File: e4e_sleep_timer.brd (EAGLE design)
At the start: 160 x 100 mm, 26 parts, among them P1 XT60, P2 10129378-906001BLF, P3 XT30PW-F, Q1 PJA3416AE_R1_00001, U1 NUCLEO-G071RB, U2 1224-5-150W

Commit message: Finished PCB review
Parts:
- removed U$5: FH-320-NV, fuses:FH-320-NV
- added Q2: PJA3416AE_R1_00001, PJA3416AE_R1_00001:SOT23_PJA3416_PNJ
- added R6: 0, rcl:R0603
- added TP11, TP12, TP13, TP14: TPTP20R, testpad:TP20R
- added U5: FH-320-NV, fuses:FH-320-NV
- moved R2 66.3 mm to (83.8, 21.6)
- moved R1 66.1 mm to (83.8, 19.1)
- moved TP8 66.0 mm to (80.0, 96.5)
- moved TP3 58.4 mm to (83.8, 96.5)
- moved U$3 53.3 mm to (101.6, 95.2)
- moved U$4 53.3 mm to (101.6, 5.08)
- moved U2 52.8 mm to (105.4, 67.3)
- moved P3 52.6 mm to (105.4, 33.0)
- moved P2 52.6 mm to (103.6, 17.8), turned to 90 degrees
- moved TP2 50.8 mm to (87.6, 96.5)
- moved TP1 43.2 mm to (91.4, 96.5)
- moved R4 40.1 mm to (85.1, 27.9), turned to 270 degrees
- moved Q1 39.9 mm to (90.2, 31.8)
- moved R3 39.3 mm to (86.0, 31.5)
- moved R5 38.6 mm to (82.5, 27.9), turned to 90 degrees
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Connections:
- removed net U5V: U1.CN10_8
- removed net VBAT: U1.CN7_33
- removed net VIN_S1: U1.CN7_24
- new net N$6: TP11.TP, U1.CN7_24
- new net N$7: R6.1, U1.CN10_32, U1.CN10_9
- new net N$8: TP13.TP, U1.CN10_8
- new net N$9: TP14.TP, U1.CN7_33
- net +5V: now also U5.2; no longer U$5.2
- net GND: now also R6.2; no longer U1.CN10_32, U1.CN10_9
- net N$2: now also Q2.1
- net N$5: now also Q2.3, TP12.TP, U5.1; no longer U$5.1
- net VDD1: now also Q2.2
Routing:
- net USART1_RXD: track 87.5 -> 10.4 mm
- net USART1_TXD: track 86.1 -> 25.4 mm
- net N$7: track 0.00 -> 54.0 mm
- net +5V: track 195.9 -> 157.1 mm
- net SYS_PWR: track 66.0 -> 29.3 mm, vias 0 -> 1
- net N$1: track 65.4 -> 37.9 mm
- net N$5: track 2.78 -> 24.4 mm
- net VEXT: track 50.1 -> 28.9 mm
- net N$8: track 0.00 -> 16.8 mm
- net N$3: track 5.63 -> 19.0 mm
- net N$6: track 0.00 -> 9.25 mm
- net N$9: track 0.00 -> 6.62 mm
- net N$2: track 4.39 -> 10.6 mm, vias 0 -> 2
- net N$4: track 7.37 -> 5.25 mm
- net VDD1: track 88.7 -> 90.5 mm
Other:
- board size 160 x 100 mm -> 107.9 x 100 mm
- board text added: "REV A"
- board text added: "Sleep Timer Board"

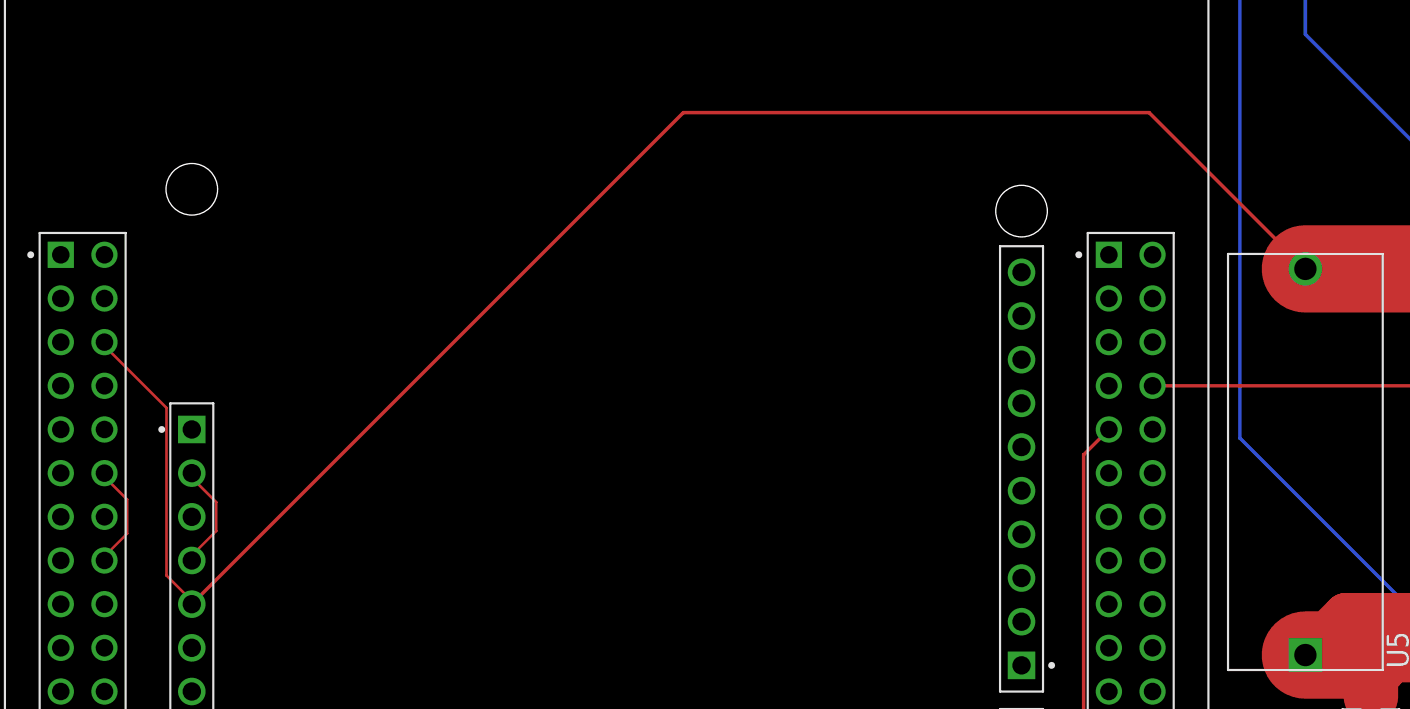
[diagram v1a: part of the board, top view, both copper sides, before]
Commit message: Added Nucleo Board power bypass
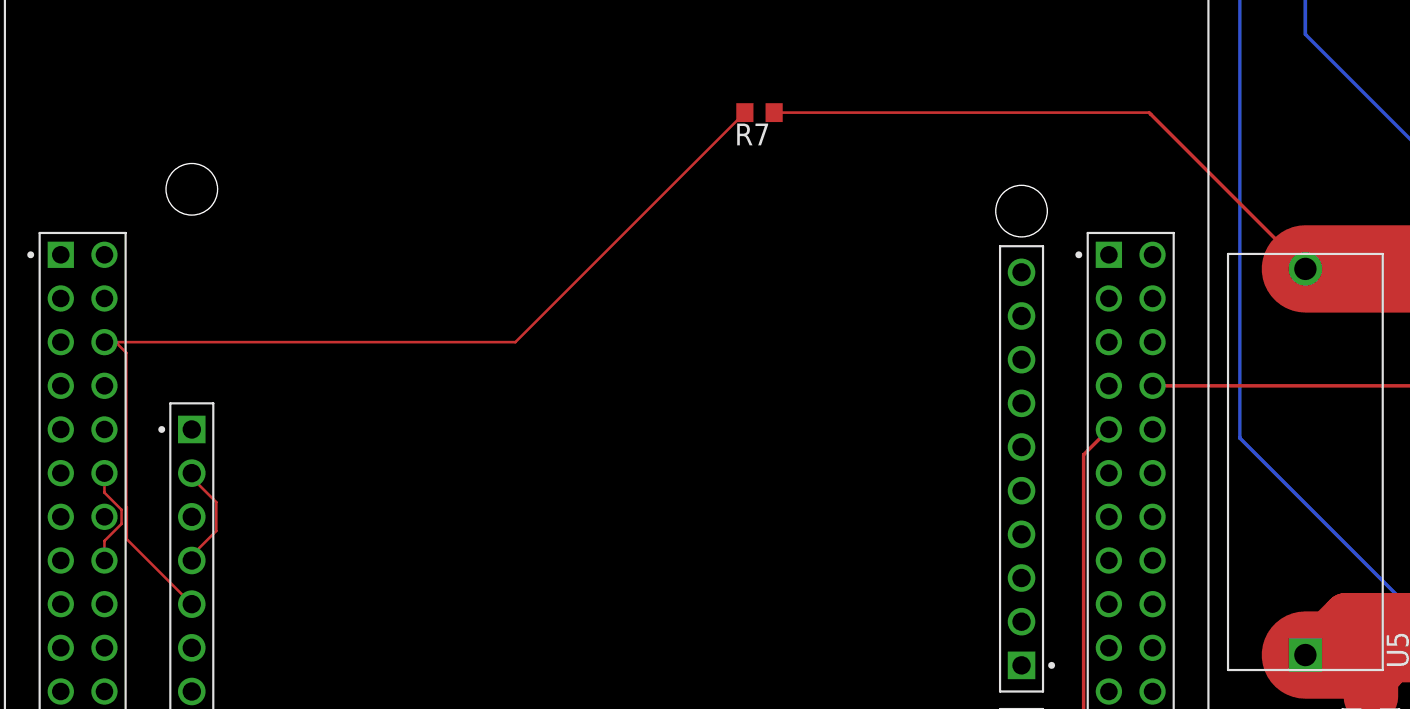
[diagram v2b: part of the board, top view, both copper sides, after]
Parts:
- added R7: 0, rcl:R0603
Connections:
- new net VDD2: R7.2, U1.CN6_5, U1.CN7_6
- net +5V: now also R7.1; no longer U1.CN6_5, U1.CN7_6
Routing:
- net +5V: track 157.1 -> 93.9 mm
- net VDD2: track 0.00 -> 60.5 mm
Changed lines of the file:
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@@
 <attribute name="VALUE" x="6.858" y="18.034" size="0.0254" layer="27"/>
+</element>
+<element name="R7" library="rcl" library_urn="urn:adsk.eagle:library:334" package="R0603" package3d_urn="urn:adsk.eagle:package:23555/3" value="0" x="54.61" y="67.31" smashed="yes" rot="R180">
+<attribute name="NAME" x="55.245" y="66.675" size="1.27" layer="25" rot="R180"/>
+<attribute name="POPULARITY" value="70" x="54.61" y="67.31" size="1.778" layer="27" rot="R180" display="off"/>
+<attribute name="SPICEPREFIX" value="R" x="54.61" y="67.31" size="1.778" layer="27" rot="R180" display="off"/>
+<attribute name="VALUE" x="55.245" y="69.215" size="1.27" layer="27" rot="R180"/>
 </element>
 </elements>
@@
 <signal name="VDD">
 <contactref element="U1" pad="CN7_5"/>
-</signal>
-<signal name="+3V3_S1">
-<contactref element="U1" pad="CN7_12"/>
-<contactref element="U1" pad="CN7_16"/>
-<wire x1="16.6116" y1="41.6052" x2="16.6116" y2="41.3004" width="0.1524" layer="1"/>
-<wire x1="17.8308" y1="42.8244" x2="16.6116" y2="41.6052" width="0.1524" layer="1"/>
-<wire x1="17.8308" y1="44.8056" x2="17.8308" y2="42.8244" width="0.1524" layer="1"/>
-<wire x1="16.6116" y1="46.0248" x2="17.8308" y2="44.8056" width="0.1524" layer="1"/>
-<wire x1="16.6116" y1="46.3296" x2="16.6116" y2="46.0248" width="0.1524" layer="1"/>
-<wire x1="16.6116" y1="41.3004" x2="16.51" y2="41.26" width="0.1524" layer="1"/>
-<wire x1="16.6116" y1="46.3296" x2="16.51" y2="46.34" width="0.1524" layer="1"/>
 </signal>
 <signal name="+5V_S1">
@@
 </signal>
 <signal name="+5V">
-<contactref element="U1" pad="CN6_5"/>
 <contactref element="U2" pad="V_OUT"/>
 <contactref element="TP2" pad="TP"/>
-<contactref element="U1" pad="CN7_6"/>
-<wire x1="16.6116" y1="53.6448" x2="16.6116" y2="53.9496" width="0.1524" layer="1"/>
-<wire x1="20.1168" y1="50.1396" x2="16.6116" y2="53.6448" width="0.1524" layer="1"/>
-<wire x1="20.1168" y1="40.386" x2="20.1168" y2="50.1396" width="0.1524" layer="1"/>
-<wire x1="21.6408" y1="38.862" x2="20.1168" y2="40.386" width="0.1524" layer="1"/>
-<wire x1="16.6116" y1="53.9496" x2="16.51" y2="53.96" width="0.1524" layer="1"/>
-<wire x1="21.6408" y1="38.862" x2="21.59" y2="38.72" width="0.1524" layer="1"/>
 <contactref element="U5" pad="2"/>
 <wire x1="86.36" y1="58.22" x2="100" y2="58.22" width="5.08" layer="1"/>
 <wire x1="100" y1="58.22" x2="100.41" y2="57.81" width="5.08" layer="1"/>
-<wire x1="86.36" y1="58.22" x2="77.27" y2="67.31" width="0.2032" layer="1"/>
-<wire x1="50.18" y1="67.31" x2="21.59" y2="38.72" width="0.2032" layer="1"/>
-<wire x1="77.27" y1="67.31" x2="50.18" y2="67.31" width="0.2032" layer="1"/>
+<wire x1="86.36" y1="58.22" x2="77.37" y2="67.21" width="0.2032" layer="1"/>
+<wire x1="77.27" y1="67.31" x2="77.37" y2="67.21" width="0.2032" layer="1"/>
 <wire x1="100.41" y1="57.81" x2="86.36" y2="71.86" width="0.2032" layer="16"/>
 <wire x1="86.36" y1="95.25" x2="87.63" y2="96.52" width="0.2032" layer="16"/>
 <wire x1="86.36" y1="71.86" x2="86.36" y2="95.25" width="0.2032" layer="16"/>
+<contactref element="R7" pad="1"/>
+<wire x1="55.46" y1="67.31" x2="77.27" y2="67.31" width="0.1524" layer="1"/>
 </signal>
 <signal name="GND">
@@
 <wire x1="13.32" y1="19.05" x2="7.62" y2="19.05" width="0.2032" layer="1"/>
 </signal>
+<signal name="+3V3_S1">
+<contactref element="U1" pad="CN7_12"/>
+<contactref element="U1" pad="CN7_16"/>
+<wire x1="17.5036" y1="44.21156875" x2="17.5036" y2="43.38843125" width="0.1524" layer="1"/>
+<wire x1="16.51" y1="46.34" x2="16.51" y2="45.20516875" width="0.1524" layer="1"/>
+<wire x1="16.51" y1="42.39483125" x2="16.51" y2="41.26" width="0.1524" layer="1"/>
+<wire x1="16.51" y1="45.20516875" x2="17.5036" y2="44.21156875" width="0.1524" layer="1"/>
+<wire x1="17.5036" y1="43.38843125" x2="16.51" y2="42.39483125" width="0.1524" layer="1"/>
+</signal>
+<signal name="VDD2">
+<contactref element="U1" pad="CN7_6"/>
+<contactref element="R7" pad="2"/>
+<contactref element="U1" pad="CN6_5"/>
+<wire x1="17.8084" y1="44.337825" x2="17.78" y2="44.366225" width="0.1524" layer="1"/>
+<wire x1="17.78" y1="44.366225" x2="17.78" y2="53.34" width="0.1524" layer="1"/>
+<wire x1="21.59" y1="38.72" x2="17.8084" y2="42.5016" width="0.1524" layer="1"/>
+<wire x1="17.8084" y1="42.5016" x2="17.8084" y2="44.337825" width="0.1524" layer="1"/>
+<wire x1="17.78" y1="53.34" x2="17.16" y2="53.96" width="0.1524" layer="1"/>
+<wire x1="17.16" y1="53.96" x2="16.51" y2="53.96" width="0.1524" layer="1"/>
+<wire x1="53.76" y1="67.31" x2="40.41" y2="53.96" width="0.1524" layer="1"/>
+<wire x1="40.41" y1="53.96" x2="16.51" y2="53.96" width="0.1524" layer="1"/>
+</signal>
 </signals>
 <mfgpreviewcolors>
@@
 <mfgpreviewcolor name="substratecolor" color="0xFF786E46"/>
 </mfgpreviewcolors>
+<errors>
+</errors>
 </board>
 </drawing>
